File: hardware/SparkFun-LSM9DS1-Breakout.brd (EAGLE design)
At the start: 22.9 x 22.9 mm, 27 parts, among them U1 LSM9DS1

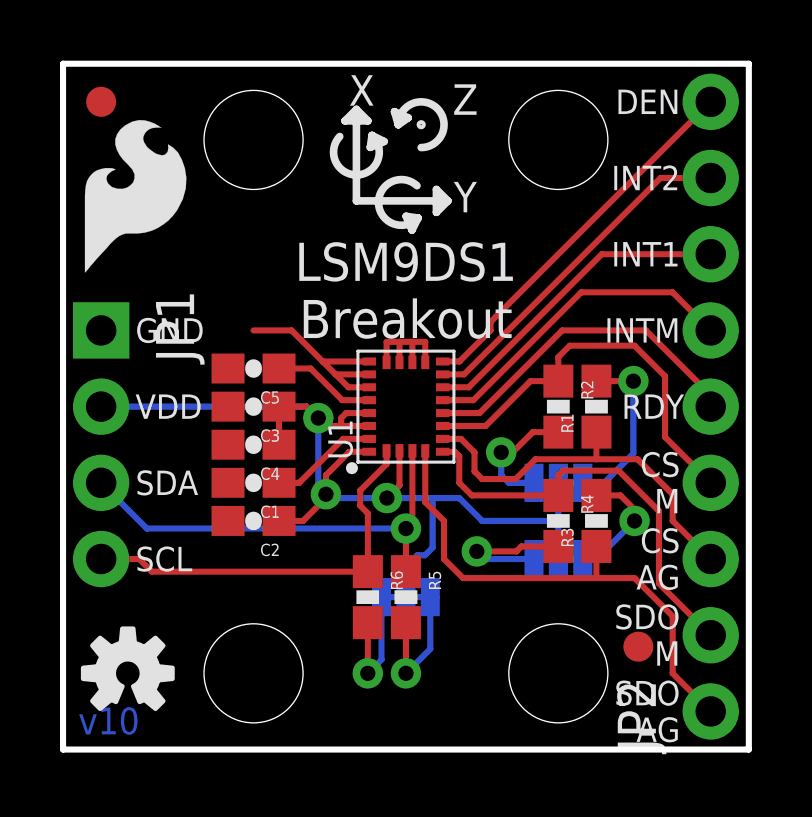
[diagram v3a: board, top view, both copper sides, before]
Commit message: Moving silk, adding GND vias, adding axis to bottom silk. Updating version to v10.
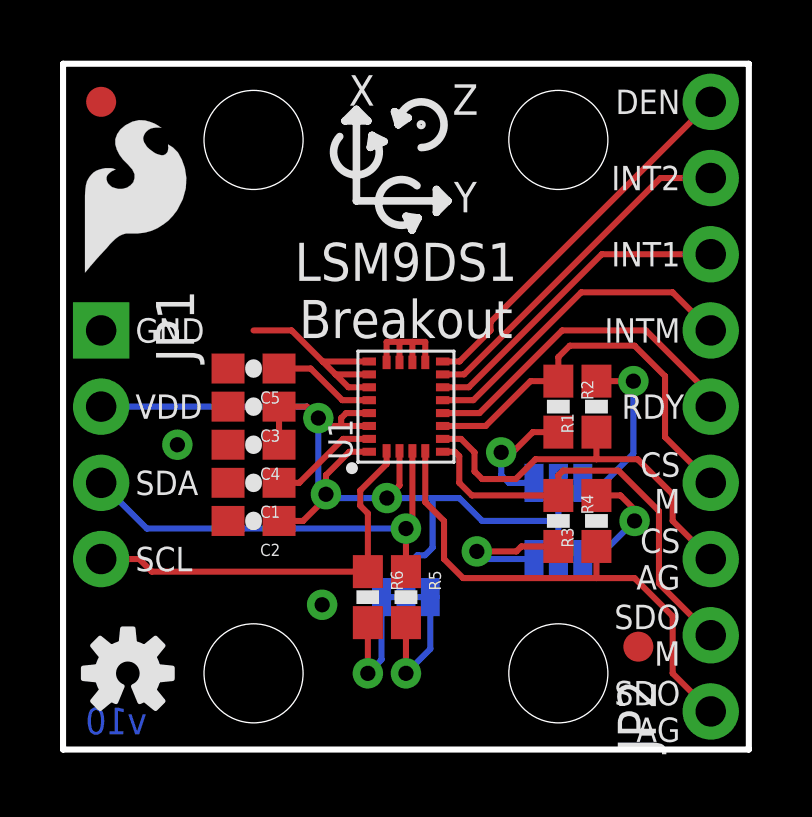
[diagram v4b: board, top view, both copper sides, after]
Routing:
- net GND: vias 0 -> 2
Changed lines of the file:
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@@
 <setting verticaltext="up"/>
 </settings>
-<grid distance="0.05" unitdist="inch" unit="inch" style="lines" multiple="1" display="yes" altdistance="0.005" altunitdist="inch" altunit="inch"/>
+<grid distance="0.05" unitdist="inch" unit="inch" style="lines" multiple="1" display="yes" altdistance="0.001" altunitdist="inch" altunit="inch"/>
 <layers>
 <layer number="1" name="Top" color="4" fill="1" visible="yes" active="yes"/>
@@
 <text x="15.621" y="10.033" size="0.8128" layer="22" font="vector" ratio="15" rot="MR0" align="bottom-center">M</text>
 <text x="17.399" y="10.033" size="0.8128" layer="22" font="vector" ratio="15" rot="MR0" align="bottom-center">AG</text>
-<text x="12.954" y="2.667" size="0.8128" layer="22" font="vector" ratio="15" rot="MR0" align="bottom-center">I</text>
-<text x="10.795" y="2.667" size="0.8128" layer="22" font="vector" ratio="15" rot="MR0" align="bottom-center">C PU</text>
-<text x="12.5095" y="3.2385" size="0.635" layer="22" font="vector" ratio="15" rot="MR0" align="bottom-center">2</text>
+<text x="12.9286" y="2.7178" size="0.8128" layer="22" font="vector" ratio="15" rot="MR0" align="bottom-center">I</text>
+<text x="10.7696" y="2.7178" size="0.8128" layer="22" font="vector" ratio="15" rot="MR0" align="bottom-center">C PU</text>
+<text x="12.4841" y="3.2893" size="0.635" layer="22" font="vector" ratio="15" rot="MR0" align="bottom-center">2</text>
 <text x="13.0556" y="17.9324" size="0.8128" layer="22" font="vector" ratio="15" rot="MR0" align="center">SDO
 0
@@
 <wire x1="16.51" y1="10.922" x2="16.51" y2="9.906" width="0.1524" layer="22"/>
 <wire x1="16.51" y1="7.874" x2="16.51" y2="7.366" width="0.1524" layer="22"/>
+<text x="1.5494" y="20.193" size="1.016" layer="22" font="vector" ratio="15" rot="MR0" align="bottom-center">X</text>
+<text x="4.953" y="17.5768" size="1.016" layer="22" font="vector" ratio="15" rot="MR180" align="bottom-center">Y</text>
+<text x="3.556" y="18.8976" size="1.016" layer="22" font="vector" ratio="15" rot="MR0" align="bottom-center">Z</text>
+<wire x1="1.651" y1="17.018" x2="4.572" y2="17.018" width="0.254" layer="22"/>
+<wire x1="1.651" y1="17.018" x2="1.651" y2="20.066" width="0.254" layer="22"/>
+<wire x1="4.572" y1="17.018" x2="4.191" y2="17.399" width="0.254" layer="22"/>
+<wire x1="4.191" y1="17.399" x2="4.191" y2="16.637" width="0.254" layer="22"/>
+<wire x1="4.191" y1="16.637" x2="4.572" y2="17.018" width="0.254" layer="22"/>
+<wire x1="2.032" y1="19.685" x2="1.651" y2="20.066" width="0.254" layer="22"/>
+<wire x1="1.27" y1="19.685" x2="2.032" y2="19.685" width="0.254" layer="22"/>
+<wire x1="1.651" y1="20.066" x2="1.27" y2="19.685" width="0.254" layer="22"/>
+<wire x1="2.6924" y1="18.796" x2="3.2004" y2="18.288" width="0.2032" layer="22"/>
+<wire x1="2.6924" y1="18.288" x2="3.2004" y2="18.796" width="0.2032" layer="22"/>
 </plain>
 <attributes>
@@
 <elements>
 <element name="FRAME1" library="SparkFun-Aesthetics" package="CREATIVE_COMMONS" value="" x="-15.24" y="-22.86" smashed="yes">
-<attribute name="VERSION" value="v10" x="0.508" y="0.508" size="0.889" layer="16" font="vector" ratio="15"/>
+<attribute name="VERSION" value="v10" x="2.794" y="0.508" size="0.889" layer="16" font="vector" ratio="15" rot="MR0"/>
 <attribute name="DESIGNER" value="Jim Lindblom" x="15.24" y="-22.86" size="1.778" layer="51" font="vector" ratio="15"/>
 </element>
@@
 <wire x1="7.62" y1="13.97" x2="6.35" y2="13.97" width="0.2032" layer="1"/>
 <wire x1="10.205" y1="12.505" x2="9.085" y2="12.505" width="0.2032" layer="1"/>
+<via x="8.636" y="4.826" extent="1-16" drill="0.508"/>
+<via x="3.81" y="10.16" extent="1-16" drill="0.508"/>
 </signal>
 <signal name="VDD">
